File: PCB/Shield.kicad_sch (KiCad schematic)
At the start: 0 parts

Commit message: Tidied schematic and layout, added indicators and silkscreen notes
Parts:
- added A1: Arduino_UNO_R3, Module:Arduino_UNO_R3, symbol MCU_Module:Arduino_UNO_R3
- added C1, C10, C11, C12, C13, C14, C15, C16, C3, C6, C7, C8, C9: 100n, Capacitor_SMD:C_0805_2012Metric_Pad1.18x1.45mm_HandSolder, symbol Device:C_Small
- added C2: 100u, Capacitor_SMD:CP_Elec_6.3x3.9, symbol Device:C_Polarized_Small
- added C4: C, Capacitor_SMD:C_0805_2012Metric_Pad1.18x1.45mm_HandSolder, symbol Device:C_Small
- added C5: 10u, Capacitor_THT:CP_Radial_D5.0mm_P2.50mm, symbol Device:C_Polarized_Small
- added D1, D11, D12, D13, D14, D15, D16, D2, D3, D5, D6, D7, D8, D9: D, Diode_SMD:D_SOD-123, symbol Device:D_Schottky
- added D10: 5V, LED_SMD:LED_0805_2012Metric_Pad1.15x1.40mm_HandSolder, symbol Device:LED
- added D17, D18, D19, D20: LED, LED_SMD:LED_0805_2012Metric_Pad1.15x1.40mm_HandSolder, symbol Device:LED
- added D21, D4: D, Diode_SMD:D_SOD-123, symbol Device:D
- added D22: APA102, LED_SMD:LED_RGB_5050-6, symbol LED:APA102
- added F1: Fuse, Fuse:Fuseholder_Clip-5x20mm_Littelfuse_111_Lateral_P18.80x5.00mm_D1.17mm_Horizontal, symbol Device:Fuse
- added J1: ADC, Connector_IDC:IDC-Header_2x10_P2.54mm_Horizontal, symbol Connector_Generic:Conn_01x20
- added J10: I2C, footprints:Molex_KK-254_1x04_P2.54mm_Horizontal, symbol Connector_Generic:Conn_01x04
- added J11: SERVO3, Connector_PinHeader_2.54mm:PinHeader_1x03_P2.54mm_Vertical, symbol Connector_Generic:Conn_01x03
- added J12: SERVO4, Connector_PinHeader_2.54mm:PinHeader_1x03_P2.54mm_Vertical, symbol Connector_Generic:Conn_01x03
- added J2: BATT, TerminalBlock:TerminalBlock_bornier-2_P5.08mm, symbol Connector:Screw_Terminal_01x02
- added J3: PWR SW, Connector_PinHeader_2.54mm:PinHeader_1x02_P2.54mm_Vertical, symbol Connector:Conn_01x02_Socket
- added J4: Screw_Terminal_01x04, TerminalBlock:TerminalBlock_bornier-4_P5.08mm, symbol Connector:Screw_Terminal_01x04
- added J5: SERVO1, Connector_PinHeader_2.54mm:PinHeader_1x03_P2.54mm_Vertical, symbol Connector_Generic:Conn_01x03
- added J6: ULTRA, footprints:Molex_KK-254_1x04_P2.54mm_Horizontal, symbol Connector_Generic:Conn_01x04
- added J7: ENC1, Connector_Molex:Molex_KK-254_AE-6410-04A_1x04_P2.54mm_Vertical, symbol Connector_Generic:Conn_01x04
- added J8: SERVO2, Connector_PinHeader_2.54mm:PinHeader_1x03_P2.54mm_Vertical, symbol Connector_Generic:Conn_01x03
- added J9: ENC2, Connector_Molex:Molex_KK-254_AE-6410-04A_1x04_P2.54mm_Vertical, symbol Connector_Generic:Conn_01x04
- added JP1, JP2, JP3, JP4, JP5, JP6: SolderJumper_2_Open, Jumper:SolderJumper-2_P1.3mm_Open_RoundedPad1.0x1.5mm, symbol Jumper:SolderJumper_2_Open
- added Q1: Q_PMOS_GDS, Package_TO_SOT_SMD:SOT-223-3_TabPin2, symbol Device:Q_PMOS_GDS
- added Q2: 2N7002DWK, Package_TO_SOT_SMD:SOT-363_SC-70-6_Handsoldering, symbol Device:Q_Dual_NMOS_S1G1D2S2G2D1
- added Q3: Q_PMOS_GDS, Package_TO_SOT_SMD:SOT-323_SC-70_Handsoldering, symbol Device:Q_PMOS_GDS
- added Q4: DualPMOS, Package_TO_SOT_SMD:SOT-23-6_Handsoldering, symbol Device:Q_Dual_PMOS_G1S2G2D2S1D1
- added R1: 10k, Resistor_SMD:R_0805_2012Metric_Pad1.20x1.40mm_HandSolder, symbol Device:R
- added R2, R3: 0R15, Resistor_SMD:R_1206_3216Metric_Pad1.30x1.75mm_HandSolder, symbol Device:R
- added R4: 150R, Resistor_SMD:R_0805_2012Metric_Pad1.20x1.40mm_HandSolder, symbol Device:R
- added R5: 2K5, Resistor_SMD:R_0805_2012Metric_Pad1.20x1.40mm_HandSolder, symbol Device:R
- added R6, R7: 100R, Resistor_SMD:R_0805_2012Metric_Pad1.20x1.40mm_HandSolder, symbol Device:R
- added R8, R9: 1K, Resistor_SMD:R_0805_2012Metric_Pad1.20x1.40mm_HandSolder, symbol Device:R
- added RN1, RN3: 10K, Resistor_SMD:R_Array_Convex_4x0603, symbol Device:R_Pack04_Split
- added RN2, RN4: 10k, Resistor_SMD:R_Array_Convex_4x0603, symbol Device:R_Pack04_Split
- added SW1: PWR SW, Button_Switch_THT:SW_E-Switch_EG2219_DPDT_Angled, symbol Switch:SW_SPST
- added SW2: SW_DIP_x01, Button_Switch_SMD:SW_DIP_SPSTx01_Slide_9.78x4.72mm_W8.61mm_P2.54mm, symbol Switch:SW_DIP_x01
- added U1: 4077, Package_SO:SOIC-14_3.9x8.7mm_P1.27mm, symbol 4xxx:4077
- added U2: NCP1117-5.0_SOT223, Package_TO_SOT_SMD:SOT-223-3_TabPin2, symbol Regulator_Linear:NCP1117-5.0_SOT223
- added U3: L298P, Package_SO:SO-20-1EP_7.52x12.825mm_P1.27mm_EP6.045x12.09mm_Mask3.56x4.47mm, symbol Driver_Motor:L298P
- added U4: LMV331, Package_TO_SOT_SMD:SOT-23-5, symbol Comparator:LMV331
- added U5: LMV358, Package_SO:SOIC-8_3.9x4.9mm_P1.27mm, symbol Amplifier_Operational:LMV358
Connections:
- new net: D4.1 (K), F1.2, Q1.3 (S), R1.1
- new net: J3.2 (Pin_2), Q1.1 (G), R1.2, SW1.2 (B)
- new net: D18.1 (K), RN3.8 (R1.2)
- new net: R9.2, RN1.1 (R1.1), U5.6 (-)
- new net: D13.2 (A), D14.1 (K), D19.2 (A), J4.1 (Pin_1), U3.16 (OUT3)
- new net: JP2.2 (B), RN1.2 (R2.1), U1.2
- new net: U1.3, U3.15 (IN4)
- new net: D21.2 (A), Q3.2 (D)
- new net: D11.2 (A), D12.1 (K), D18.2 (A), J4.4 (Pin_4), U3.5 (OUT2)
- new net: Q2.6 (D), Q3.1 (G), RN4.4 (R4.1)
- new net: JP6.1 (A), RN1.8 (R1.2), U5.7
- new net: D17.1 (K), RN3.7 (R2.2)
- new net: D22.1 (DI), JP3.2 (B)
- new net: D22.2 (CI), JP4.2 (B)
- new net: Q2.1 (S), Q2.5 (G), RN4.3 (R3.1), SW2.2
- new net: Q2.2 (G), R6.2
- new net: Q4.1 (G), R7.2
- new net: Q4.4 (D), Q4.6 (D)
- new net: JP1.2 (B), RN1.3 (R3.1), U1.5
- new net: JP5.1 (A), RN1.5 (R4.2), U5.1
- new net: R8.2, RN1.4 (R4.1), U5.2 (-)
- new net: R5.1, RN2.6 (R3.2), U4.3 (-)
- new net: RN2.7 (R2.2), RN2.8 (R1.2), U4.1 (+)
- new net: D15.2 (A), D16.1 (K), D20.2 (A), J4.2 (Pin_2), U3.17 (OUT4)
- new net: D17.2 (A), D8.2 (A), D9.1 (K), J4.3 (Pin_3), U3.4 (OUT1)
- new net: U1.4, U3.9 (IN2)
- new net: F1.1, J2.1 (Pin_1)
- new net: D20.1 (K), RN3.6 (R3.2)
- new net: D19.1 (K), RN3.5 (R4.2)
- new net: R6.1, RN2.5 (R4.2), U4.4
- new net: Q2.3 (D), Q4.3 (G), RN4.2 (R2.1)
- new net: D10.1 (K), R4.1
- new net +5V: C1.2, C10.1, C11.1, C12.1, C13.1, C14.1, C15.2, C16.2, C3.2, C4.2, C5.1, C6.2, C7.1, C8.1, C9.1, D10.2 (A), D22.4 (VCC), J1.10 (Pin_10), J1.13 (Pin_13), J1.16 (Pin_16), J1.19 (Pin_19), J1.4 (Pin_4), J1.7 (Pin_7), J10.4 (Pin_4), J11.2 (Pin_2), J12.2 (Pin_2), J5.2 (Pin_2), J6.4 (Pin_4), J7.1 (Pin_1), J8.2 (Pin_2), J9.1 (Pin_1), Q4.2 (S), RN2.1 (R1.1), RN2.4 (R4.1), RN4.6 (R3.2), RN4.7 (R2.2), U1.14 (VDD), U2.2 (VO), U3.12 (Vss), U4.5 (V+), U5.8 (V+)
- new net +BATT: C2.1, D11.1 (K), D13.1 (K), D15.1 (K), D8.1 (K), Q1.2 (D), Q3.3 (S), RN2.3 (R3.1), RN4.5 (R4.2), U2.3 (VI), U3.6 (Vs)
- new net AIN0: A1.9 (A0), D1.2 (A), J1.20 (Pin_20), JP5.2 (B)
- new net AIN1: A1.10 (A1), D2.2 (A), J1.17 (Pin_17), JP6.2 (B)
- new net AIN2: A1.11 (A2), D3.2 (A), J1.14 (Pin_14)
- new net AIN3: A1.12 (A3), D5.2 (A), J1.11 (Pin_11)
- new net AIN4: A1.13 (SDA/A4), D6.2 (A), J1.8 (Pin_8)
- new net AIN5: A1.14 (SCL/A5), D7.2 (A), J1.5 (Pin_5)
- new net BRKA: A1.22 (D7), J6.3 (Pin_3), JP1.1 (A)
- new net BRKB: A1.23 (D8), J6.2 (Pin_2), JP2.1 (A)
- new net DIRA: A1.18 (D3), J12.1 (Pin_1), U1.6, U3.7 (IN1)
- new net DIRB: A1.27 (D12), U1.1, U3.13 (IN3)
- new net ENC1A: A1.16 (D1/TX), J7.2 (Pin_2)
- new net ENC1B: A1.15 (D0/RX), J7.3 (Pin_3)
- new net ENC2A: A1.17 (D2), J9.2 (Pin_2)
- new net ENC2B: A1.19 (D4), J9.3 (Pin_3)
- new net GND: A1.29 (GND), A1.6 (GND), A1.7 (GND), C1.1, C10.2, C11.2, C12.2, C13.2, C14.2, C15.1, C16.1, C2.2, C3.1, C4.1, C5.2, C6.1, C7.2, C8.2, C9.2, D12.2 (A), D14.2 (A), D16.2 (A), D22.3 (GND), D4.2 (A), D9.2 (A), J1.1 (Pin_1), J1.12 (Pin_12), J1.15 (Pin_15), J1.18 (Pin_18), J1.2 (Pin_2), J1.3 (Pin_3), J1.6 (Pin_6), J1.9 (Pin_9), J10.1 (Pin_1), J11.3 (Pin_3), J12.3 (Pin_3), J2.2 (Pin_2), J3.1 (Pin_1), J5.3 (Pin_3), J6.1 (Pin_1), J7.4 (Pin_4), J8.3 (Pin_3), J9.4 (Pin_4), Q2.4 (S), R2.2, R3.2, R4.2, R5.2, R8.1, R9.1, RN1.6 (R3.2), RN1.7 (R2.2), RN2.2 (R2.1), RN3.1 (R1.1), RN3.2 (R2.1), RN3.3 (R3.1), RN3.4 (R4.1), SW1.1 (A), SW2.1, U1.7 (VSS), U2.1 (GND), U3.1 (GND), U3.10 (GND), U3.11 (GND), U3.20 (GND), U4.2 (V-), U5.4 (V-)
- new net IOREF: A1.2 (IOREF), D1.1 (K), D2.1 (K), D3.1 (K), D5.1 (K), D6.1 (K), D7.1 (K)
- new net MOSI: A1.26 (D11), J11.1 (Pin_1), JP3.1 (A)
- new net MTRA: A1.24 (D9), U3.8 (EnA)
- new net MTRB: A1.25 (D10), U3.14 (EnB)
- new net SCK: A1.28 (D13), JP4.1 (A)
- new net SCL: A1.31 (SDA/A4), J10.3 (Pin_3)
- new net SDA: A1.32 (SCL/A5), J10.2 (Pin_2)
- new net SENA: R2.1, U3.2 (SENSE_A), U5.3 (+)
- new net SENB: R3.1, U3.19 (SENSE_B), U5.5 (+)
- new net SERVO1: A1.20 (D5), J5.1 (Pin_1)
- new net SERVO2: A1.21 (D6), J8.1 (Pin_1)
- new net Vin: A1.8 (VIN), D21.1 (K), Q4.5 (S), R7.1
- new net uC_3V3: A1.4 (3V3)
- new net uC_5V: A1.5 (+5V)
- no-connect marks 0 -> 4
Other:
- removed sheet uC
- note added: "Add series Ilimit resistors?"
- note added: "Change E caps to SMD?"
- note added: "NEW"
- note added: "why to IOREF?"
- note removed: "Depth sensing: - Pressure transducer? - Ultrasonics? - Capacitive?"
- note removed: "Temp sensing: - thermistor? - thermocouple?"

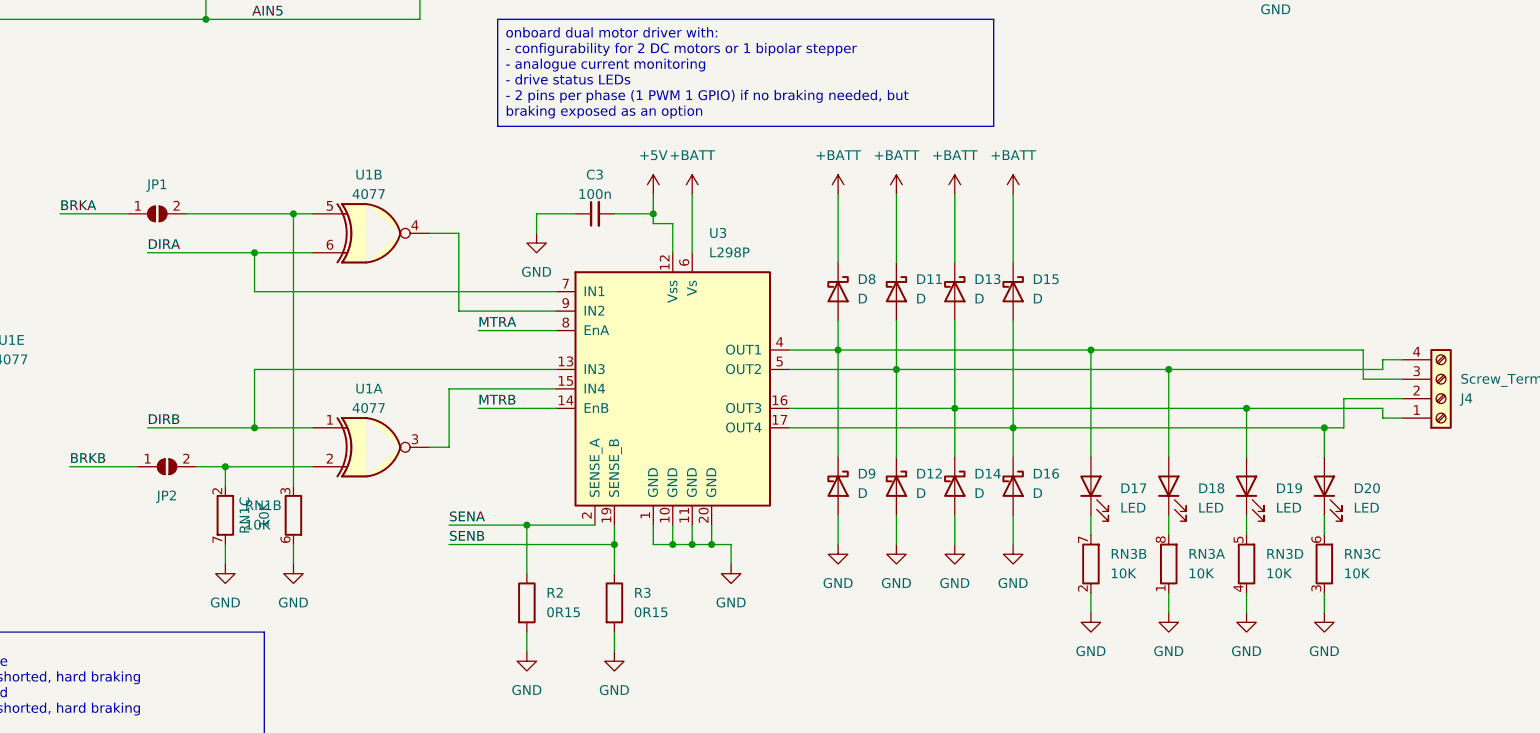
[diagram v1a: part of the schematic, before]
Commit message: Fixed links between schem and pcb, re-added annotation, updated L298 footprint and updated layout
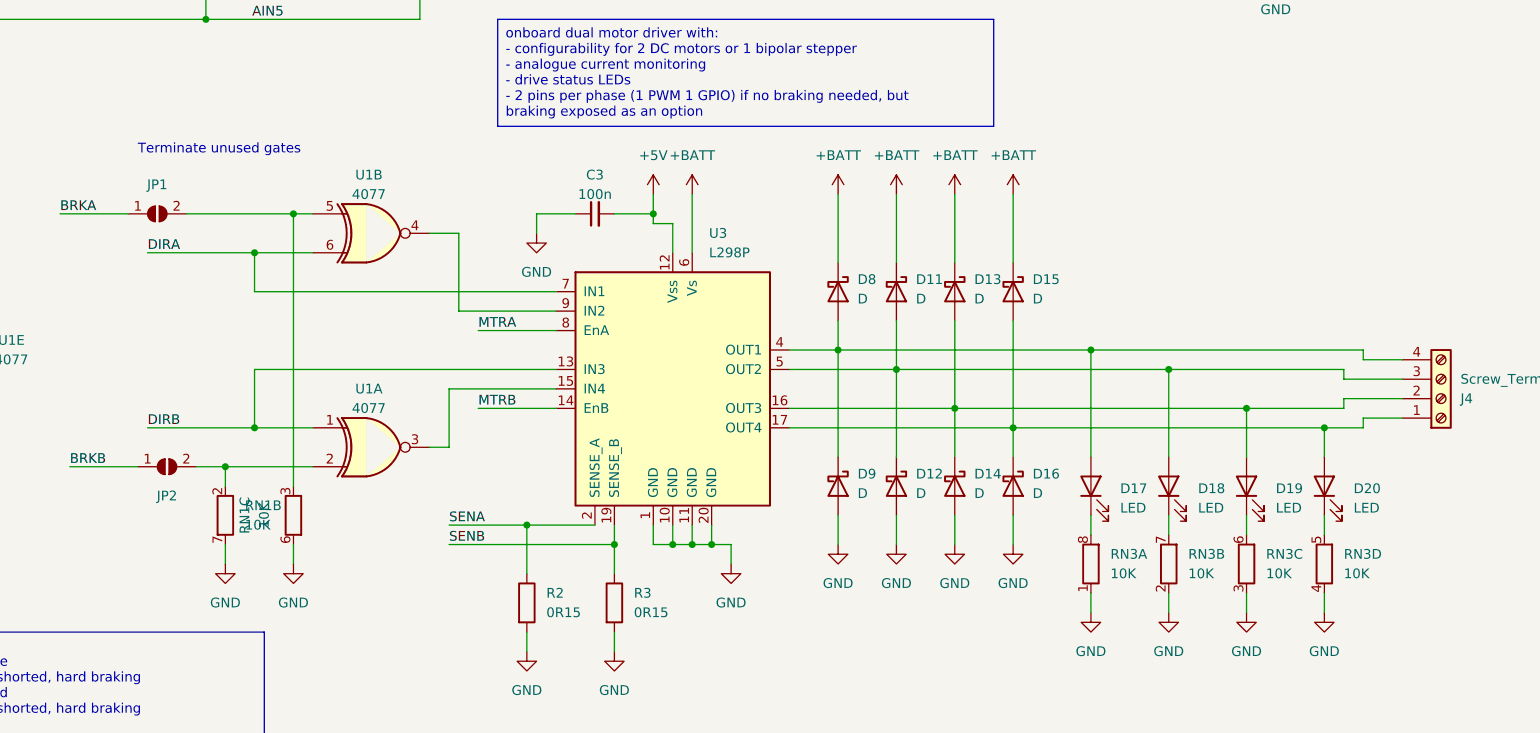
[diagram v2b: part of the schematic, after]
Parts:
- C2: footprint Capacitor_SMD:CP_Elec_6.3x3.9 -> Capacitor_THT:CP_Radial_D5.0mm_P2.50mm
- U3: footprint Package_SO:SO-20-1EP_7.52x12.825mm_P1.27mm_EP6.045x12.09mm_Mask3.56x4.47mm -> footprints:SOIC127P1420X360-21N
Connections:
- net at D18.1 (K): now also RN3.7 (R2.2); no longer RN3.8 (R1.2)
- net at D13.2 (A), D14.1 (K), D19.2 (A)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: now also J4.2 (Pin_2); no longer J4.1 (Pin_1)
- net at D11.2 (A), D12.1 (K), D18.2 (A)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: now also J4.3 (Pin_3); no longer J4.4 (Pin_4)
- net at D17.1 (K): now also RN3.8 (R1.2); no longer RN3.7 (R2.2)
- net at D15.2 (A), D16.1 (K), D20.2 (A)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: now also J4.1 (Pin_1); no longer J4.2 (Pin_2)
- net at D17.2 (A), D8.2 (A), D9.1 (K)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: now also J4.4 (Pin_4); no longer J4.3 (Pin_3)
- net at D20.1 (K): now also RN3.5 (R4.2); no longer RN3.6 (R3.2)
- net at D19.1 (K): now also RN3.6 (R3.2); no longer RN3.5 (R4.2)
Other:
- note added: "Terminate unused gates"

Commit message: Added comment
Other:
- note added: "Add pos/neg input protection for all GPIO?"
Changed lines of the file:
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@@
+    (effects (font (size 1.27 1.27)) (justify left bottom))
+  )
+  (text "Add pos/neg input protection for all GPIO?" (at 210.82 96.52 0)
     (effects (font (size 1.27 1.27)) (justify left bottom))
   )
